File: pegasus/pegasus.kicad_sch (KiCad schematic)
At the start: 10 parts, among them IC1 RFD900, IC2 Adafruit_MPL3115A2, IC3 Adafruit-BNO055-PCB, IC4 L70B-M39, IC5 L7805ACV, J1 Conn_01x02_Female, J2 Conn_01x02_Female, U1 Teensy4.1, U2 CON-SMA-EDGE-S, U3 CON-SMA-EDGE-S

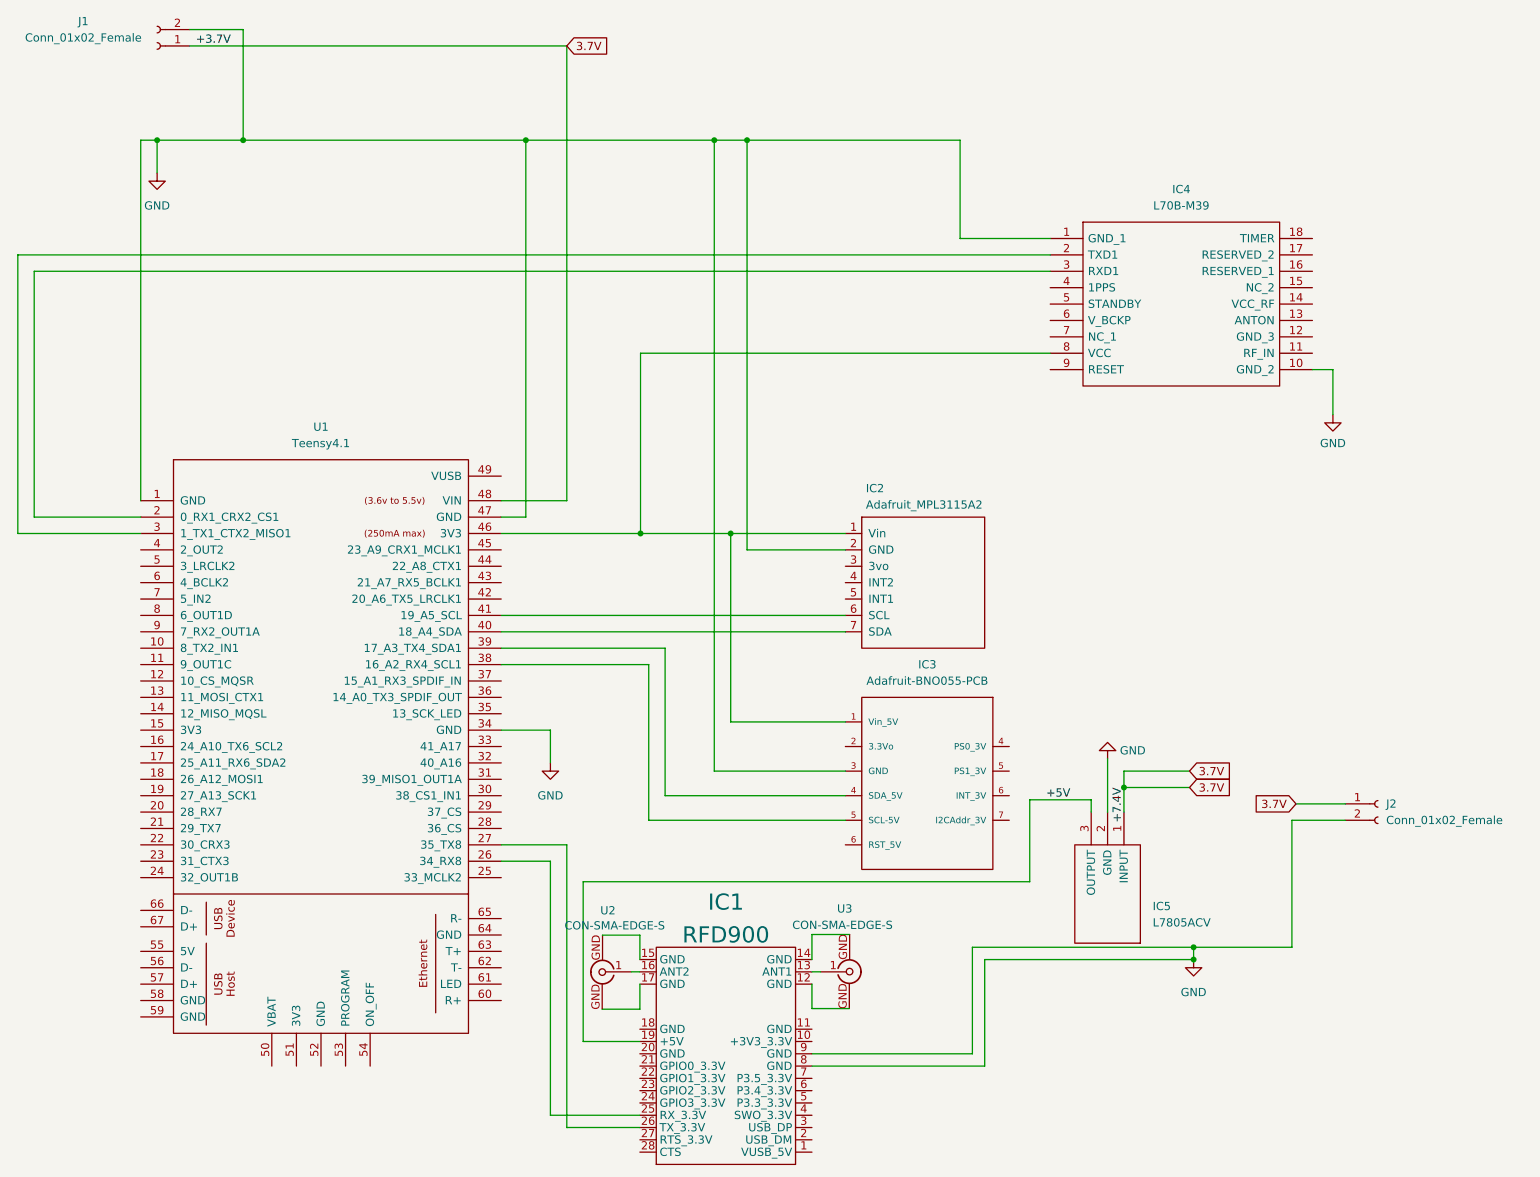
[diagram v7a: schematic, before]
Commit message: fixed UART wiring for gps and modem
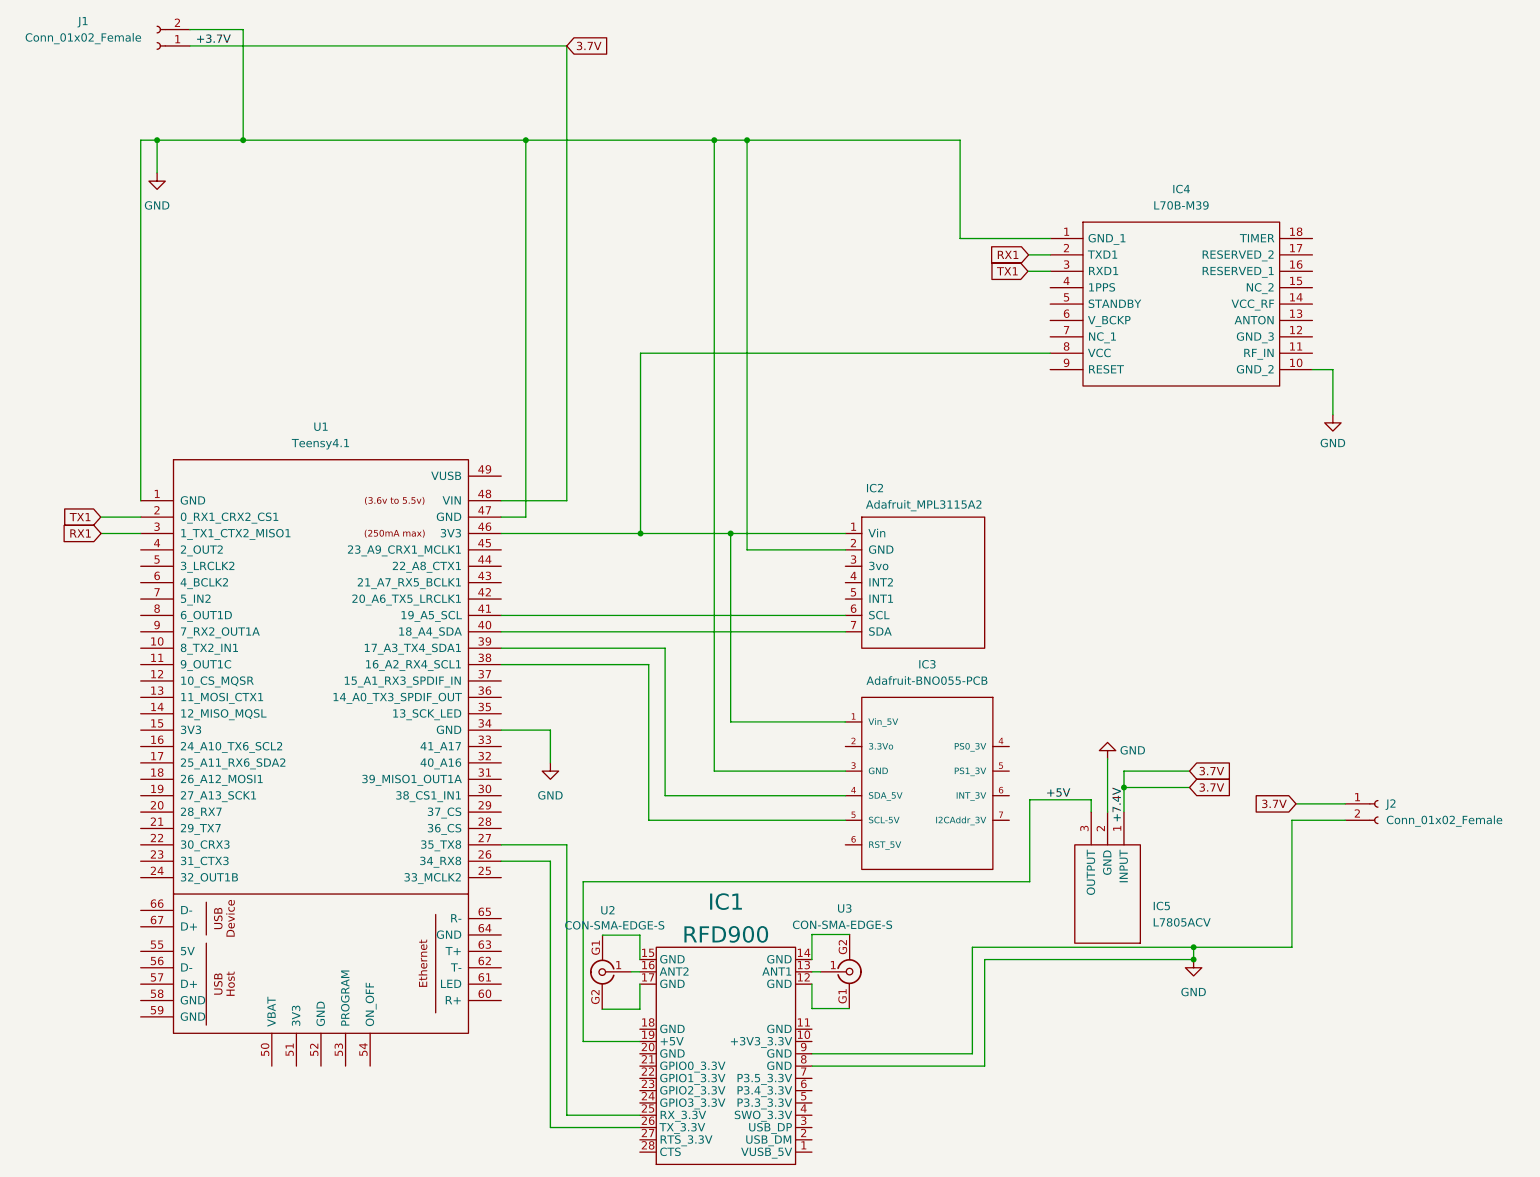
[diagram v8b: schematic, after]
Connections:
- net TX1: now reaches IC4.3 (RXD1), U1.2 (0_RX1_CRX2_CS1)
- net at U1.26 (34_RX8): now also IC1.26 (TX_3.3V); no longer IC1.25 (RX_3.3V)
- net at U1.27 (35_TX8): now also IC1.25 (RX_3.3V); no longer IC1.26 (TX_3.3V)
- net RX1: now reaches IC4.2 (TXD1), U1.3 (1_TX1_CTX2_MISO1)
- net at IC1.15 (GND): now also U2.G1; no longer U2.GND
- net at IC1.17 (GND): now also U2.G2; no longer U2.GND
- net at IC1.12 (GND): now also U3.G1; no longer U3.GND
- net at IC1.14 (GND): now also U3.G2; no longer U3.GND
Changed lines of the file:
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@@
     (stroke (width 0) (type default) (color 0 0 0 0))
   )
-  (wire (pts (xy 105.41 186.69) (xy 105.41 147.32))
+  (wire (pts (xy 105.41 147.32) (xy 105.41 188.595))
     (stroke (width 0) (type default) (color 0 0 0 0))
   )
@@
     (stroke (width 0) (type default) (color 0 0 0 0))
   )
-  (wire (pts (xy 41.91 93.98) (xy 25.4 93.98))
-    (stroke (width 0) (type default) (color 0 0 0 0))
-  )
-  (wire (pts (xy 22.86 96.52) (xy 22.86 53.34))
+  (wire (pts (xy 179.5272 53.34) (xy 182.88 53.34))
     (stroke (width 0) (type default) (color 0 0 0 0))
   )
@@
     (stroke (width 0) (type default) (color 0 0 0 0))
   )
+  (wire (pts (xy 35.7124 93.98) (xy 41.91 93.98))
+    (stroke (width 0) (type default) (color 0 0 0 0))
+  )
   (wire (pts (xy 226.695 71.12) (xy 226.695 78.105))
     (stroke (width 0) (type default) (color 0 0 0 0))
@@
     (stroke (width 0) (type default) (color 0 0 0 0))
   )
-  (wire (pts (xy 25.4 55.88) (xy 182.88 55.88))
-    (stroke (width 0) (type default) (color 0 0 0 0))
-  )
-  (wire (pts (xy 107.95 188.595) (xy 119.2784 188.595))
-    (stroke (width 0) (type default) (color 0 0 0 0))
-  )
   (wire (pts (xy 120.65 116.84) (xy 97.79 116.84))
     (stroke (width 0) (type default) (color 0 0 0 0))
@@
     (stroke (width 0) (type default) (color 0 0 0 0))
   )
+  (wire (pts (xy 179.4256 55.88) (xy 182.88 55.88))
+    (stroke (width 0) (type default) (color 0 0 0 0))
+  )
+  (wire (pts (xy 107.95 186.69) (xy 119.2784 186.69))
+    (stroke (width 0) (type default) (color 0 0 0 0))
+  )
   (wire (pts (xy 97.79 96.52) (xy 119.38 96.52))
     (stroke (width 0) (type default) (color 0 0 0 0))
   )
-  (wire (pts (xy 107.95 188.595) (xy 107.95 144.78))
+  (wire (pts (xy 107.95 144.78) (xy 107.95 186.69))
     (stroke (width 0) (type default) (color 0 0 0 0))
   )
@@
     (stroke (width 0) (type default) (color 0 0 0 0))
   )
+  (wire (pts (xy 105.41 188.595) (xy 119.2784 188.595))
+    (stroke (width 0) (type default) (color 0 0 0 0))
+  )
   (wire (pts (xy 135.89 35.56) (xy 135.89 99.06))
     (stroke (width 0) (type default) (color 0 0 0 0))
@@
     (stroke (width 0) (type default) (color 0 0 0 0))
   )
-  (wire (pts (xy 41.91 96.52) (xy 22.86 96.52))
-    (stroke (width 0) (type default) (color 0 0 0 0))
-  )
-  (wire (pts (xy 105.41 186.69) (xy 119.2784 186.69))
-    (stroke (width 0) (type default) (color 0 0 0 0))
-  )
   (wire (pts (xy 101.6 93.98) (xy 101.6 35.56))
     (stroke (width 0) (type default) (color 0 0 0 0))
@@
     (stroke (width 0) (type default) (color 0 0 0 0))
   )
+  (wire (pts (xy 35.7632 96.52) (xy 41.91 96.52))
+    (stroke (width 0) (type default) (color 0 0 0 0))
+  )
   (wire (pts (xy 191.77 131.445) (xy 191.77 139.7))
     (stroke (width 0) (type default) (color 0 0 0 0))
@@
     (stroke (width 0) (type default) (color 0 0 0 0))
   )
-  (wire (pts (xy 22.86 53.34) (xy 182.88 53.34))
-    (stroke (width 0) (type default) (color 0 0 0 0))
-  )
   (wire (pts (xy 44.45 35.56) (xy 44.45 40.64))
     (stroke (width 0) (type default) (color 0 0 0 0))
@@
   )
   (wire (pts (xy 145.9484 170.1546) (xy 145.9484 166.37))
-    (stroke (width 0) (type default) (color 0 0 0 0))
-  )
-  (wire (pts (xy 25.4 93.98) (xy 25.4 55.88))
     (stroke (width 0) (type default) (color 0 0 0 0))
   )
@@
   (label "+7.4V" (at 194.31 135.89 270)
     (effects (font (size 1.27 1.27)) (justify right bottom))
+  )
+  (global_label "TX1" (shape input) (at 179.4256 55.88 180) (fields_autoplaced)
+    (effects (font (size 1.27 1.27)) (justify right))
+    (property "Intersheet References" "${INTERSHEET_REFS}" (id 0) (at 173.6258 55.8006 0)
+      (effects (font (size 1.27 1.27)) (justify right) hide)
+    )
+  )
+  (global_label "RX1" (shape input) (at 35.7632 96.52 180) (fields_autoplaced)
+    (effects (font (size 1.27 1.27)) (justify right))
+    (property "Intersheet References" "${INTERSHEET_REFS}" (id 0) (at 29.6611 96.4406 0)
+      (effects (font (size 1.27 1.27)) (justify right) hide)
+    )
   )
   (global_label "3.7V" (shape input) (at 220.98 138.43 180) (fields_autoplaced)
@@
     (property "Intersheet References" "${INTERSHEET_REFS}" (id 0) (at 210.9955 133.2706 0)
       (effects (font (size 1.27 1.27)) (justify left) hide)
+    )
+  )
+  (global_label "RX1" (shape input) (at 179.5272 53.34 180) (fields_autoplaced)
+    (effects (font (size 1.27 1.27)) (justify right))
+    (property "Intersheet References" "${INTERSHEET_REFS}" (id 0) (at 173.4251 53.2606 0)
+      (effects (font (size 1.27 1.27)) (justify right) hide)
+    )
+  )
+  (global_label "TX1" (shape input) (at 35.7124 93.98 180) (fields_autoplaced)
+    (effects (font (size 1.27 1.27)) (justify right))
+    (property "Intersheet References" "${INTERSHEET_REFS}" (id 0) (at 29.9126 93.9006 0)
+      (effects (font (size 1.27 1.27)) (justify right) hide)
     )
   )
@@
     )
     (pin "1")
-    (pin "GND")
-    (pin "GND")
+    (pin "G1")
+    (pin "G2")
   )
   (symbol (lib_id "Adafruit_MPL3115A2:Adafruit_MPL3115A2") (at 134.9375 102.5525 0) (unit 1)
@@
     (pin "9")
   )
-  (symbol (lib_id "sma-connectors:CON-SMA-EDGE-S") (at 156.8704 164.5666 270) (unit 1)
+  (symbol (lib_name "CON-SMA-EDGE-S_2") (lib_id "sma-connectors:CON-SMA-EDGE-S") (at 156.8704 164.5666 270) (unit 1)
     (in_bom yes) (on_board yes)
     (property "Reference" "U3" (id 0) (at 149.8346 154.686 90)
@@
     )
     (pin "1")
-    (pin "GND")
-    (pin "GND")
+    (pin "G1")
+    (pin "G2")
   )
   (sheet_instances
